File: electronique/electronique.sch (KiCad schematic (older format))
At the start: 9 parts, among them U1 STM32L451RETx

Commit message: Schema change
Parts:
- added J1: Conn_02x07_Odd_Even, FTSH:SAMTEC_FTSH-107-01-L-DV-K-A, symbol Connector_Generic:Conn_02x07_Odd_Even
- added R?: R, symbol Device:R
- added SW2: Rotary_Encoder, symbol Device:Rotary_Encoder
- added U2: LD1117S50TR_SOT223, Package_TO_SOT_SMD:SOT-223-3_TabPin2, symbol Regulator_Linear:LD1117S50TR_SOT223
- added U3: LD1117S33TR_SOT223, Package_TO_SOT_SMD:SOT-223-3_TabPin2, symbol Regulator_Linear:LD1117S33TR_SOT223
- added U? (x2): LB1930MC-AH, SOIC10_3P9X4P9_ONS, symbol lumos-minima:LB1930MC-AH
- BT1: renamed from BT?; value Battery_Cell -> 7.2V
- gave numbers to parts that had none: 7
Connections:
- net labels added: +3.3V, +5V, NRST, RX1, SWCLK, SWDIO, TX1
- wire segments 12 -> 45
- no-connect marks 0 -> 5
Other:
- moved on the sheet: BT1, C1, C2, D1, Y1

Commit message: Schema change
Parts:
- removed M1, M2: Motor_DC, symbol Motor:Motor_DC
- removed SW1, SW2: Rotary_Encoder, symbol Device:Rotary_Encoder
- removed U?: LB1930MC-AH, SOIC10_3P9X4P9_ONS, symbol lumos-minima:LB1930MC-AH
- added J10: PHOTOD3, symbol Connector_Generic:Conn_01x02
- added J11: PHOTOD4, symbol Connector_Generic:Conn_01x02
- added J12: Ultrason 3, symbol Connector_Generic:Conn_01x04
- added J13: Moteur 2, symbol Connector_Generic:Conn_01x06
- added J14: Moteur 1, symbol Connector_Generic:Conn_01x06
- added J2: Conn_01x02, symbol Connector_Generic:Conn_01x02
- added J3: Camera, symbol Connector_Generic:Conn_01x06
- added J4: TOF1, symbol Connector_Generic:Conn_02x05_Odd_Even
- added J5: Conn_01x06, symbol Connector_Generic:Conn_01x06
- added J6: Ultrason 1, symbol Connector_Generic:Conn_01x04
- added J7: PHOTOD1, symbol Connector_Generic:Conn_01x02
- added J8: PHOTOD2, symbol Connector_Generic:Conn_01x02
- added J9: Ultrason 2, symbol Connector_Generic:Conn_01x04
- added R10, R11, R2, R3, R4, R5, R6, R7: R, Resistor_SMD:R_0805_2012Metric_Pad1.20x1.40mm_HandSolder, symbol Device:R
- added R8, R9: R, symbol Device:R
- added U4: LB1930MC-AH, symbol lumos-minima:LB1930MC-AH
- R1: renamed from R?; footprint (none) -> Resistor_SMD:R_0805_2012Metric_Pad1.20x1.40mm_HandSolder
- U5: renamed from U?; footprint SOIC10_3P9X4P9_ONS -> (none)
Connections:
- net labels added: +BATT, CS, ECHO1, ECHO2, ECHO3, LED_A, LED_B, LED_C, M1N_PWM, M1_A, M1_B, M1_PWM, M2N_PWM, M2_A, M2_B, M2_PWM, MISO, MOSI, PHOTOD, PHOTOD1, PHOTOD2, PHOTOD3, PHOTOD4, SCK, SCL, SDA, TRIG_US, XSHUT
- wire segments 45 -> 196
- no-connect marks 5 -> 10
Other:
- moved on the sheet: BT1, C1, C2, D1, U1, U2, U3, U5, Y1

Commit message: Schema mis a jour pour la seance de projet
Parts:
- C1, C2: footprint (none) -> Capacitor_SMD:C_0805_2012Metric_Pad1.15x1.40mm_HandSolder
- R8, R9: footprint (none) -> Resistor_THT:R_Axial_DIN0207_L6.3mm_D2.5mm_P7.62mm_Horizontal
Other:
- moved on the sheet: J1, R1
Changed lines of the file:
@@
 EESchema Schematic File Version 4
-EELAYER 30 0
+LIBS:electronique-cache
+EELAYER 29 0
 EELAYER END
 $Descr A4 11693 8268
@@
 F 0 "C1" V 4052 2300 50  0000 C CNN
 F 1 "C" V 3961 2300 50  0000 C CNN
-F 2 "" H 3838 2150 50  0001 C CNN
+F 2 "Capacitor_SMD:C_0805_2012Metric_Pad1.15x1.40mm_HandSolder" H 3838 2150 50  0001 C CNN
 F 3 "~" H 3800 2300 50  0001 C CNN
 	1    3800 2300
@@
 F 0 "C2" V 3548 2800 50  0000 C CNN
 F 1 "C" V 3639 2800 50  0000 C CNN
-F 2 "" H 3838 2650 50  0001 C CNN
+F 2 "Capacitor_SMD:C_0805_2012Metric_Pad1.15x1.40mm_HandSolder" H 3838 2650 50  0001 C CNN
 F 3 "~" H 3800 2800 50  0001 C CNN
 	1    3800 2800
@@
 L Connector_Generic:Conn_02x07_Odd_Even J1
 U 1 1 615F66B1
-P 1550 4800
-F 0 "J1" H 1600 5317 50  0000 C CNN
-F 1 "Conn_02x07_Odd_Even" H 1600 5226 50  0000 C CNN
-F 2 "FTSH:SAMTEC_FTSH-107-01-L-DV-K-A" H 1550 4800 50  0001 C CNN
-F 3 "~" H 1550 4800 50  0001 C CNN
-	1    1550 4800
+P 2250 2700
+F 0 "J1" H 2300 3217 50  0000 C CNN
+F 1 "Conn_02x07_Odd_Even" H 2300 3126 50  0000 C CNN
+F 2 "FTSH:SAMTEC_FTSH-107-01-L-DV-K-A" H 2250 2700 50  0001 C CNN
+F 3 "~" H 2250 2700 50  0001 C CNN
+	1    2250 2700
 	1    0    0    -1
 $EndComp
@@
 	1    0    0    -1
 $EndComp
-NoConn ~ 1350 4500
-NoConn ~ 1850 4500
-NoConn ~ 1850 4800
-NoConn ~ 1850 4900
-NoConn ~ 1350 4900
+NoConn ~ 2050 2400
+NoConn ~ 2550 2400
+NoConn ~ 2550 2700
+NoConn ~ 2550 2800
+NoConn ~ 2050 2800
 $Comp
 L power:GND #PWR0106
 U 1 1 6161C108
-P 850 4750
-F 0 "#PWR0106" H 850 4500 50  0001 C CNN
-F 1 "GND" V 855 4622 50  0000 R CNN
-F 2 "" H 850 4750 50  0001 C CNN
-F 3 "" H 850 4750 50  0001 C CNN
-	1    850  4750
+P 1550 2650
+F 0 "#PWR0106" H 1550 2400 50  0001 C CNN
+F 1 "GND" V 1555 2522 50  0000 R CNN
+F 2 "" H 1550 2650 50  0001 C CNN
+F 3 "" H 1550 2650 50  0001 C CNN
+	1    1550 2650
 	0    1    1    0
 $EndComp
 Wire Wire Line
-	1350 4700 1250 4700
-Wire Wire Line
-	1250 4700 1250 4750
-Wire Wire Line
-	1250 4800 1350 4800
-Wire Wire Line
-	1250 4750 850  4750
-Connection ~ 1250 4750
-Wire Wire Line
-	1250 4750 1250 4800
+	2050 2600 1950 2600
+Wire Wire Line
+	1950 2600 1950 2650
+Wire Wire Line
+	1950 2700 2050 2700
+Wire Wire Line
+	1950 2650 1550 2650
+Connection ~ 1950 2650
+Wire Wire Line
+	1950 2650 1950 2700
 $Comp
 L power:GND #PWR0107
 U 1 1 6161D905
-P 850 5000
-F 0 "#PWR0107" H 850 4750 50  0001 C CNN
-F 1 "GND" V 855 4872 50  0000 R CNN
-F 2 "" H 850 5000 50  0001 C CNN
-F 3 "" H 850 5000 50  0001 C CNN
-	1    850  5000
+P 1550 2900
+F 0 "#PWR0107" H 1550 2650 50  0001 C CNN
+F 1 "GND" V 1555 2772 50  0000 R CNN
+F 2 "" H 1550 2900 50  0001 C CNN
+F 3 "" H 1550 2900 50  0001 C CNN
+	1    1550 2900
 	0    1    1    0
 $EndComp
@@
 L Device:R R1
 U 1 1 6161E3ED
-P 1050 5000
-F 0 "R1" V 950 5000 50  0000 C CNN
-F 1 "R" V 850 5000 50  0000 C CNN
-F 2 "Resistor_SMD:R_0805_2012Metric_Pad1.20x1.40mm_HandSolder" V 980 5000 50  0001 C CNN
-F 3 "~" H 1050 5000 50  0001 C CNN
-	1    1050 5000
+P 1750 2900
+F 0 "R1" V 1650 2900 50  0000 C CNN
+F 1 "R" V 1550 2900 50  0000 C CNN
+F 2 "Resistor_SMD:R_0805_2012Metric_Pad1.20x1.40mm_HandSolder" V 1680 2900 50  0001 C CNN
+F 3 "~" H 1750 2900 50  0001 C CNN
+	1    1750 2900
 	0    1    -1   0
 $EndComp
 Wire Wire Line
-	1200 5000 1350 5000
-Wire Wire Line
-	900  5000 850  5000
-Wire Wire Line
-	1850 4600 2200 4600
-Wire Wire Line
-	1850 4700 2200 4700
-Text Label 2200 4600 2    50   ~ 0
+	1900 2900 2050 2900
+Wire Wire Line
+	1600 2900 1550 2900
+Wire Wire Line
+	2550 2500 2900 2500
+Wire Wire Line
+	2550 2600 2900 2600
+Text Label 2900 2500 2    50   ~ 0
 SWDIO
-Text Label 2200 4700 2    50   ~ 0
+Text Label 2900 2600 2    50   ~ 0
 SWCLK
 Wire Wire Line
-	1850 5000 2200 5000
-Text Label 2200 5000 2    50   ~ 0
+	2550 2900 2900 2900
+Text Label 2900 2900 2    50   ~ 0
 NRST
 Wire Wire Line
-	1850 5100 2200 5100
-Text Label 2200 5100 2    50   ~ 0
+	2550 3000 2900 3000
+Text Label 2900 3000 2    50   ~ 0
 TX1
 Wire Wire Line
-	1350 5100 1200 5100
-Text Label 1200 5100 0    50   ~ 0
+	2050 3000 1900 3000
+Text Label 1900 3000 0    50   ~ 0
 RX1
 $Comp
 L power:+3.3V #PWR0108
 U 1 1 616474D0
-P 850 4600
-F 0 "#PWR0108" H 850 4450 50  0001 C CNN
-F 1 "+3.3V" H 865 4773 50  0000 C CNN
-F 2 "" H 850 4600 50  0001 C CNN
-F 3 "" H 850 4600 50  0001 C CNN
-	1    850  4600
+P 1550 2500
+F 0 "#PWR0108" H 1550 2350 50  0001 C CNN
+F 1 "+3.3V" H 1565 2673 50  0000 C CNN
+F 2 "" H 1550 2500 50  0001 C CNN
+F 3 "" H 1550 2500 50  0001 C CNN
+	1    1550 2500
 	0    -1   -1   0
 $EndComp
 Wire Wire Line
-	850  4600 1350 4600
+	1550 2500 2050 2500
 Text Label 6450 3000 2    50   ~ 0
 SWCLK
@@
 F 0 "R9" V 9443 1050 50  0000 C CNN
 F 1 "R" V 9534 1050 50  0000 C CNN
-F 2 "" V 9580 1050 50  0001 C CNN
+F 2 "Resistor_THT:R_Axial_DIN0207_L6.3mm_D2.5mm_P7.62mm_Horizontal" V 9580 1050 50  0001 C CNN
 F 3 "~" H 9650 1050 50  0001 C CNN
 	1    9650 1050
@@
 F 0 "R8" V 9393 2300 50  0000 C CNN
 F 1 "R" V 9484 2300 50  0000 C CNN
-F 2 "" V 9530 2300 50  0001 C CNN
+F 2 "Resistor_THT:R_Axial_DIN0207_L6.3mm_D2.5mm_P7.62mm_Horizontal" V 9530 2300 50  0001 C CNN
 F 3 "~" H 9600 2300 50  0001 C CNN
 	1    9600 2300

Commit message: Schema/Routage presque finis
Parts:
- added C1, C11, C12, C3, C5, C7: .1uF, Capacitor_SMD:C_0805_2012Metric_Pad1.18x1.45mm_HandSolder, symbol Device:C
- added C13, C2, C4, C6, C8: 10uF, Capacitor_Tantalum_SMD:CP_EIA-2012-12_Kemet-R_Pad1.30x1.05mm_HandSolder, symbol Device:CP
- added C14: 1uF, Capacitor_Tantalum_SMD:CP_EIA-2012-12_Kemet-R_Pad1.30x1.05mm_HandSolder, symbol Device:CP
- added C15: .01uF, Capacitor_SMD:C_0805_2012Metric_Pad1.18x1.45mm_HandSolder, symbol Device:C
- added FB1: Ferrite_Bead_Small, Ferrite_THT:LairdTech_28C0236-0JW-10, symbol Device:Ferrite_Bead_Small
- added SW1: SW_Push, Button_Switch_THT:SW_PUSH_6mm, symbol Switch:SW_Push
- J10, J11, J7, J8: footprint (none) -> Connector_JST:JST_PH_B2B-PH-K_1x02_P2.00mm_Vertical
- J12, J6, J9: footprint (none) -> Connector_PinHeader_2.54mm:PinHeader_1x04_P2.54mm_Vertical
- J13, J14: footprint (none) -> Connector_JST:JST_PH_B6B-PH-K_1x06_P2.00mm_Vertical
- U4, U5: footprint (none) -> lumos_minima:LB1930MC-AH
- renumbered C2 to C10, C1 to C9, J2 to J1, J1 to J2, U2 to U1, U3 to U2, U1 to U3
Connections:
- net +3V3: now also U3.1 (VBAT), U3.48 (VDDUSB), C1.1, C12.1, C13.1, C2.1, C3.1, C4.1, C5.1, C6.1, C7.1, C8.1, FB1.2; no longer U3.13 (VDDA)
- net GND: now also C1.2, C11.2, C12.2, C13.2, C14.2, C15.2, C2.2, C3.2, C4.2, C5.2, C6.2, C7.2, C8.2, SW1.2
- net NRST: now also C11.1, SW1.1
- new net VDDA: C14.1, C15.1, FB1.1, U3.13 (VDDA)
- no-connect marks 10 -> 36

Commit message: Schema/Routage presque finis
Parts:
- BT1: footprint (none) -> Connector_PinHeader_2.54mm:PinHeader_2x01_P2.54mm_Vertical
- J1: footprint (none) -> Connector_JST:JST_PH_B2B-PH-K_1x02_P2.00mm_Vertical
- J3, J5: footprint (none) -> Connector_PinHeader_2.54mm:PinHeader_1x06_P2.54mm_Vertical
- J4: footprint (none) -> Connector_PinHeader_2.54mm:PinHeader_2x05_P2.54mm_Vertical
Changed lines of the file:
@@
 F 0 "BT1" H 1668 1396 50  0000 L CNN
 F 1 "7.2V" H 1668 1305 50  0000 L CNN
-F 2 "" V 1550 1360 50  0001 C CNN
+F 2 "Connector_PinHeader_2.54mm:PinHeader_2x01_P2.54mm_Vertical" V 1550 1360 50  0001 C CNN
 F 3 "~" V 1550 1360 50  0001 C CNN
 	1    1550 1300
@@
 F 0 "J1" H 1080 1292 50  0000 L CNN
 F 1 "Conn_01x02" H 1080 1201 50  0000 L CNN
-F 2 "" H 1000 1300 50  0001 C CNN
+F 2 "Connector_JST:JST_PH_B2B-PH-K_1x02_P2.00mm_Vertical" H 1000 1300 50  0001 C CNN
 F 3 "~" H 1000 1300 50  0001 C CNN
 	1    1000 1300
@@
 F 0 "J3" H 6980 892 50  0000 L CNN
 F 1 "Camera" H 6980 801 50  0000 L CNN
-F 2 "" H 6900 900 50  0001 C CNN
+F 2 "Connector_PinHeader_2.54mm:PinHeader_1x06_P2.54mm_Vertical" H 6900 900 50  0001 C CNN
 F 3 "~" H 6900 900 50  0001 C CNN
 	1    6900 900
@@
 F 0 "J5" H 8330 4692 50  0000 L CNN
 F 1 "Conn_01x06" H 8330 4601 50  0000 L CNN
-F 2 "" H 8250 4700 50  0001 C CNN
+F 2 "Connector_PinHeader_2.54mm:PinHeader_1x06_P2.54mm_Vertical" H 8250 4700 50  0001 C CNN
 F 3 "~" H 8250 4700 50  0001 C CNN
 	1    8250 4700
@@
 F 0 "J4" H 7900 3867 50  0000 C CNN
 F 1 "TOF1" H 7900 3776 50  0000 C CNN
-F 2 "" H 7850 3450 50  0001 C CNN
+F 2 "Connector_PinHeader_2.54mm:PinHeader_2x05_P2.54mm_Vertical" H 7850 3450 50  0001 C CNN
 F 3 "~" H 7850 3450 50  0001 C CNN
 	1    7850 3450
@@
 Wire Wire Line
 	4750 1600 4550 1600
-$Comp
-L MCU_ST_STM32L4:STM32L451RETx U3
-U 1 1 61570DC1
-P 5450 3200
-F 0 "U3" H 5400 1311 50  0000 C CNN
-F 1 "STM32L451RETx" H 5400 1220 50  0000 C CNN
-F 2 "Package_QFP:LQFP-64_10x10mm_P0.5mm" H 4850 1500 50  0001 R CNN
-F 3 "http://www.st.com/st-web-ui/static/active/en/resource/technical/document/datasheet/DM00340475.pdf" H 5450 3200 50  0001 C CNN
-	1    5450 3200
-	1    0    0    -1
-$EndComp
 NoConn ~ 7650 3650
 NoConn ~ 8150 3650
@@
 NoConn ~ 4750 2900
 NoConn ~ 3900 5200
+$Comp
+L MCU_ST_STM32L4:STM32L451RETx U3
+U 1 1 61570DC1
+P 5450 3200
+F 0 "U3" H 5400 1311 50  0000 C CNN
+F 1 "STM32L451RETx" H 5400 1220 50  0000 C CNN
+F 2 "Package_QFP:LQFP-64_10x10mm_P0.5mm" H 4850 1500 50  0001 R CNN
+F 3 "http://www.st.com/st-web-ui/static/active/en/resource/technical/document/datasheet/DM00340475.pdf" H 5450 3200 50  0001 C CNN
+	1    5450 3200
+	1    0    0    -1
+$EndComp
 $EndSCHEMATC

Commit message: Ajout de l'ampli de captage de courant MAX40056.
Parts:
- added U6, U7: MAX40056FAUA+, Package_SO:MSOP-8_3x3mm_P0.65mm, symbol lumos-minima:MAX40056FAUA+
- R8, R9: value R -> 30m; footprint Resistor_THT:R_Axial_DIN0207_L6.3mm_D2.5mm_P7.62mm_Horizontal -> Resistor_SMD:R_1206_3216Metric_Pad1.30x1.75mm_HandSolder
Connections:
- no-connect marks 36 -> 35
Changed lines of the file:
@@
 P 9650 1050
 F 0 "R9" V 9443 1050 50  0000 C CNN
-F 1 "R" V 9534 1050 50  0000 C CNN
-F 2 "Resistor_THT:R_Axial_DIN0207_L6.3mm_D2.5mm_P7.62mm_Horizontal" V 9580 1050 50  0001 C CNN
+F 1 "30m" V 9534 1050 50  0000 C CNN
+F 2 "Resistor_SMD:R_1206_3216Metric_Pad1.30x1.75mm_HandSolder" V 9580 1050 50  0001 C CNN
 F 3 "~" H 9650 1050 50  0001 C CNN
 	1    9650 1050
@@
 P 9600 2300
 F 0 "R8" V 9393 2300 50  0000 C CNN
-F 1 "R" V 9484 2300 50  0000 C CNN
-F 2 "Resistor_THT:R_Axial_DIN0207_L6.3mm_D2.5mm_P7.62mm_Horizontal" V 9530 2300 50  0001 C CNN
+F 1 "30m" V 9484 2300 50  0000 C CNN
+F 2 "Resistor_SMD:R_1206_3216Metric_Pad1.30x1.75mm_HandSolder" V 9530 2300 50  0001 C CNN
 F 3 "~" H 9600 2300 50  0001 C CNN
 	1    9600 2300
@@
 NoConn ~ 6050 1600
 NoConn ~ 4750 2900
-NoConn ~ 3900 5200
 $Comp
 L MCU_ST_STM32L4:STM32L451RETx U3
@@
 	1    0    0    -1
 $EndComp
+$Comp
+L lumos-minima:MAX40056FAUA+ U6
+U 1 1 617AB703
+P 3250 5400
+F 0 "U6" H 3250 6170 50  0000 C CNN
+F 1 "MAX40056FAUA+" H 3250 6079 50  0000 C CNN
+F 2 "Package_SO:MSOP-8_3x3mm_P0.65mm" H 3250 5400 50  0001 L BNN
+F 3 "" H 3250 5400 50  0001 L BNN
+F 4 "SOP65P490X110-8N" H 3250 5400 50  0001 L BNN "Package"
+	1    3250 5400
+	1    0    0    -1
+$EndComp
+$Comp
+L lumos-minima:MAX40056FAUA+ U7
+U 1 1 617C6A16
+P 3250 6900
+F 0 "U7" H 3250 7670 50  0000 C CNN
+F 1 "MAX40056FAUA+" H 3250 7579 50  0000 C CNN
+F 2 "Package_SO:MSOP-8_3x3mm_P0.65mm" H 3250 6900 50  0001 L BNN
+F 3 "" H 3250 6900 50  0001 L BNN
+F 4 "SOP65P490X110-8N" H 3250 6900 50  0001 L BNN "Package"
+	1    3250 6900
+	1    0    0    -1
+$EndComp

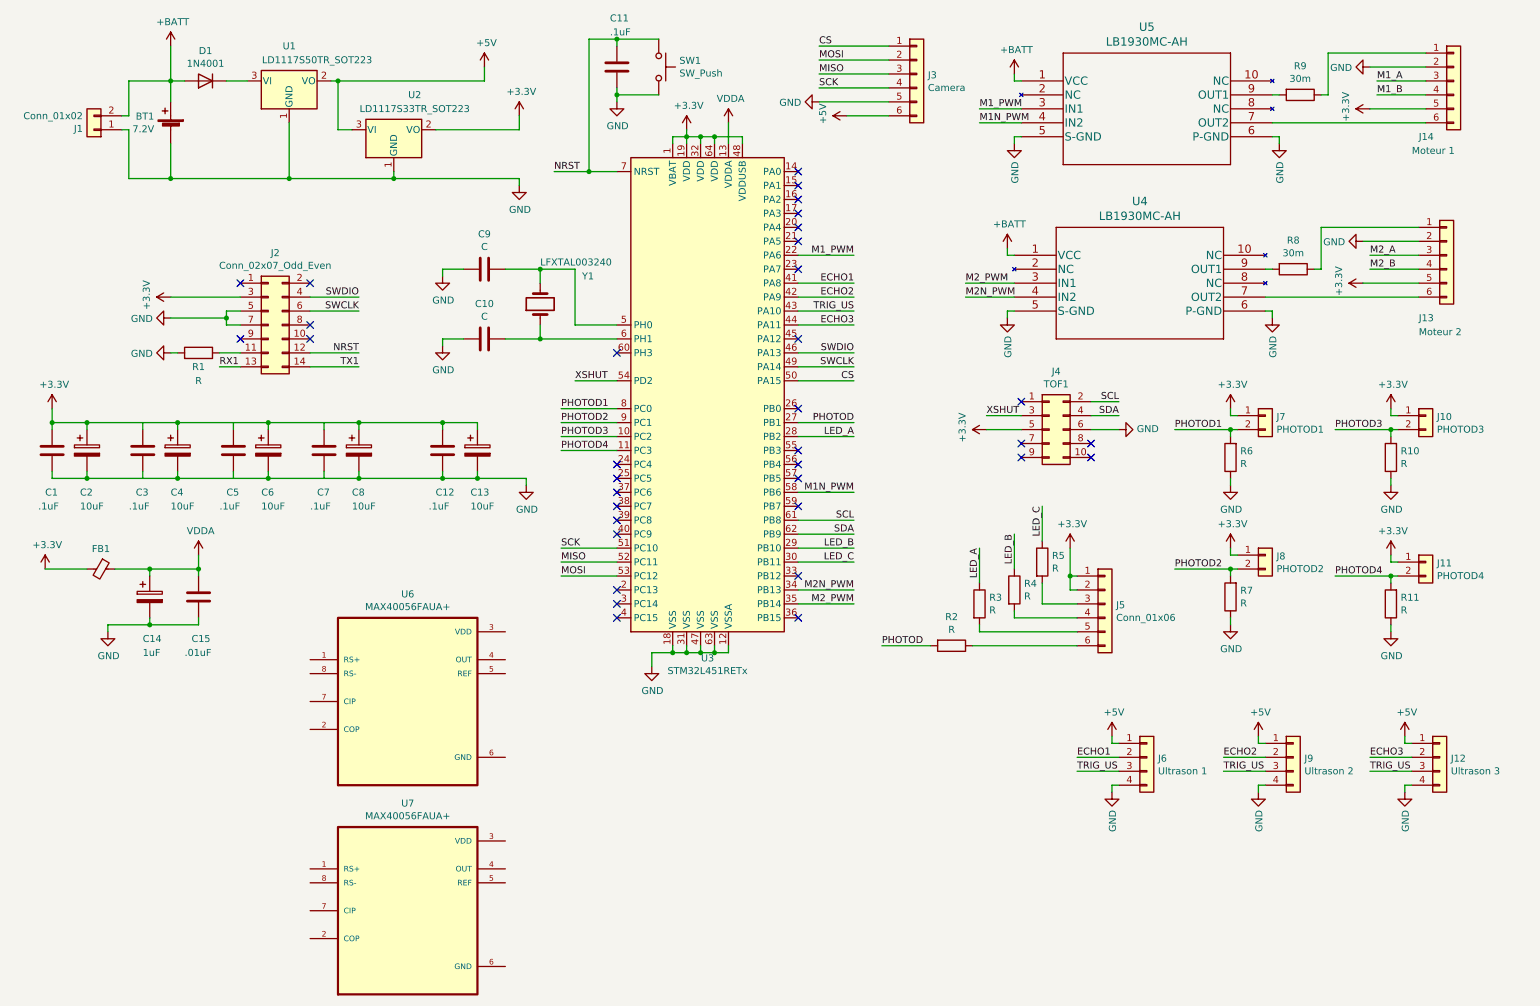
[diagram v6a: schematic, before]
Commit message: Cablage preliminaire des capteurs de courant
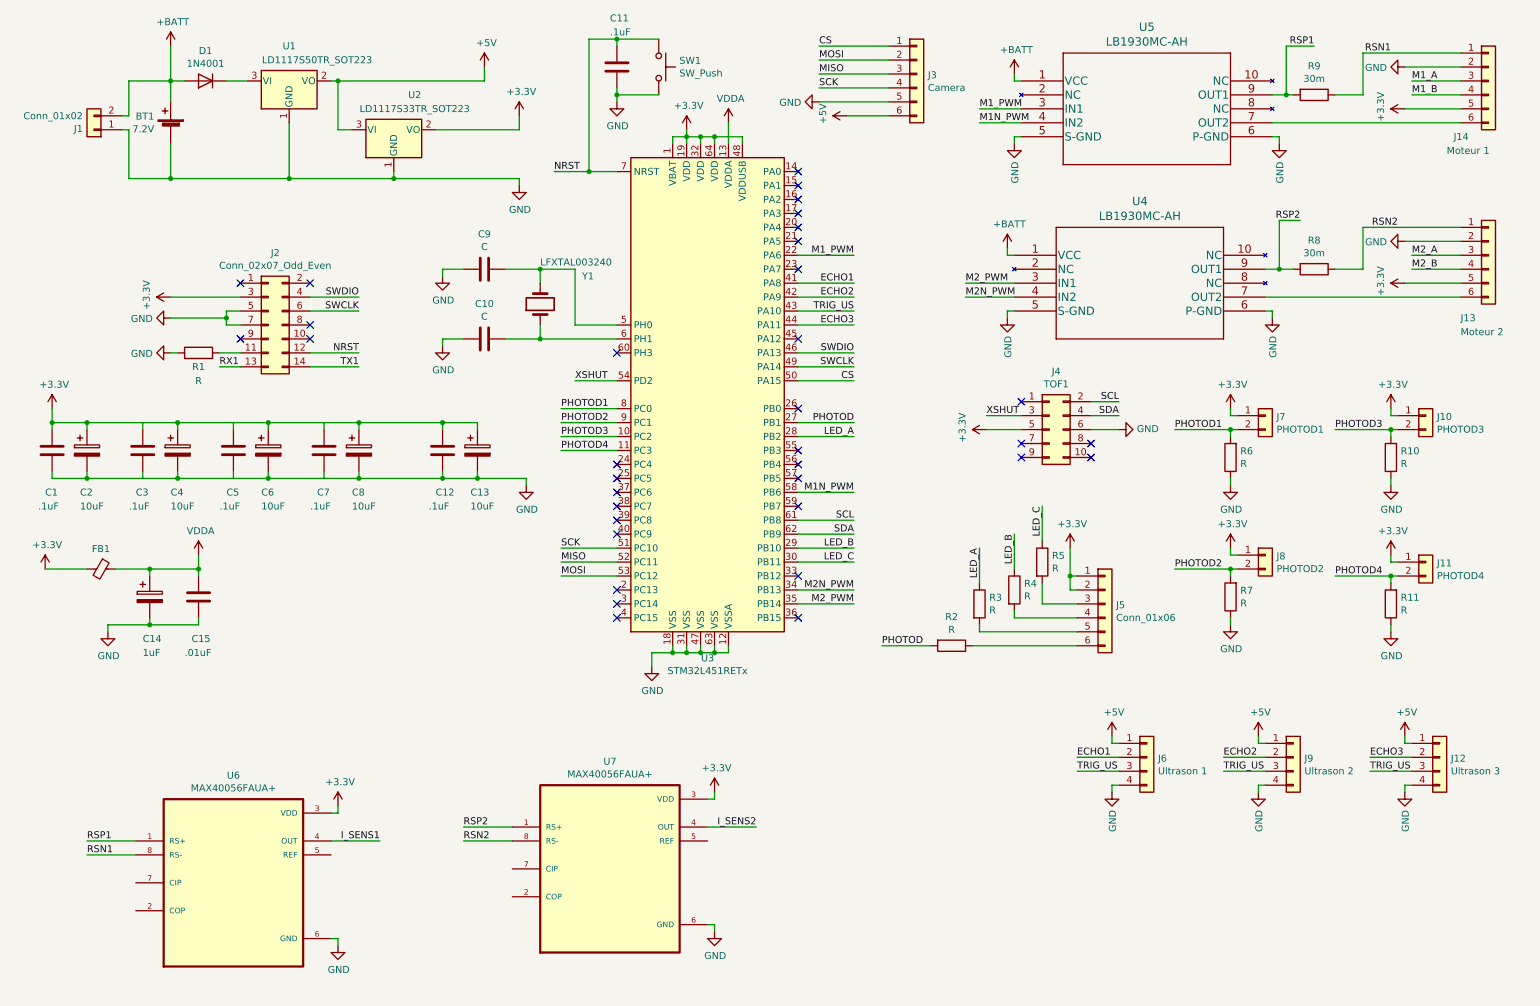
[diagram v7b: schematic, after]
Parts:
- J2: footprint FTSH:SAMTEC_FTSH-107-01-L-DV-K-A -> lumos_minima:SAMTEC_FTSH-107-01-L-DV-K-A
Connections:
- net +3V3: now also U6.3 (VDD), U7.3 (VDD)
- net GND: now also U6.6 (GND), U7.6 (GND)
- net RSP1: now reaches R9.2, U5.9 (OUT1)
- net RSP1: now also U6.1 (RS+)
- net RSN1: now reaches J14.1 (Pin_1), R9.1
- net RSN1: now also U6.8 (RS-)
- net I_SENS1: now reaches U6.4 (OUT)
- net RSP2: now reaches U7.1 (RS+)
- net RSP2: now also R8.2, U4.9 (OUT1)
- net I_SENS2: now reaches U7.4 (OUT)
- net RSN2: now reaches U7.8 (RS-)
- net RSN2: now also J13.1 (Pin_1), R8.1
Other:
- moved on the sheet: J13, J14, R8, R9, U6, U7
